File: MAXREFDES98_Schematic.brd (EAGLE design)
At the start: 64.6 x 25.4 mm, 15 parts, among them T1 TG110-S055N2RL

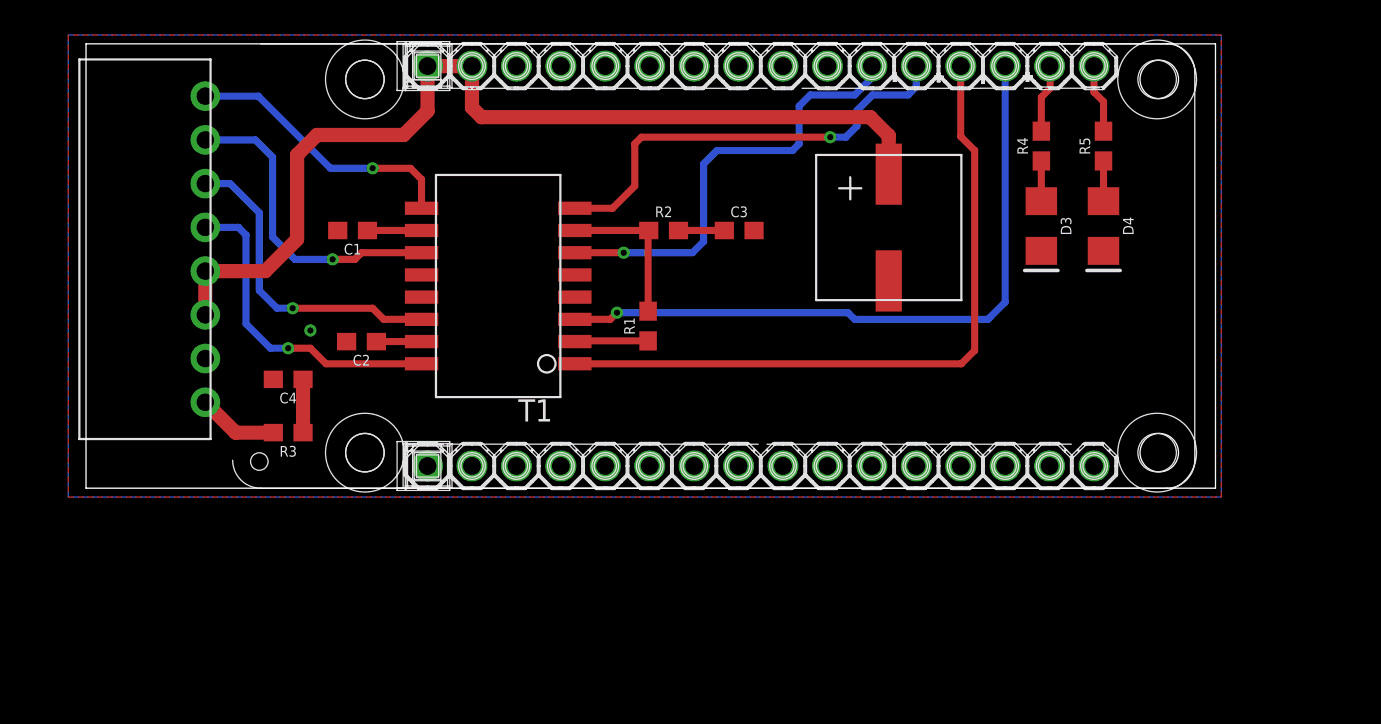
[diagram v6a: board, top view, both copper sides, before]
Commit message: Added schematic labels, 1206 cap, fixed ethernet line width
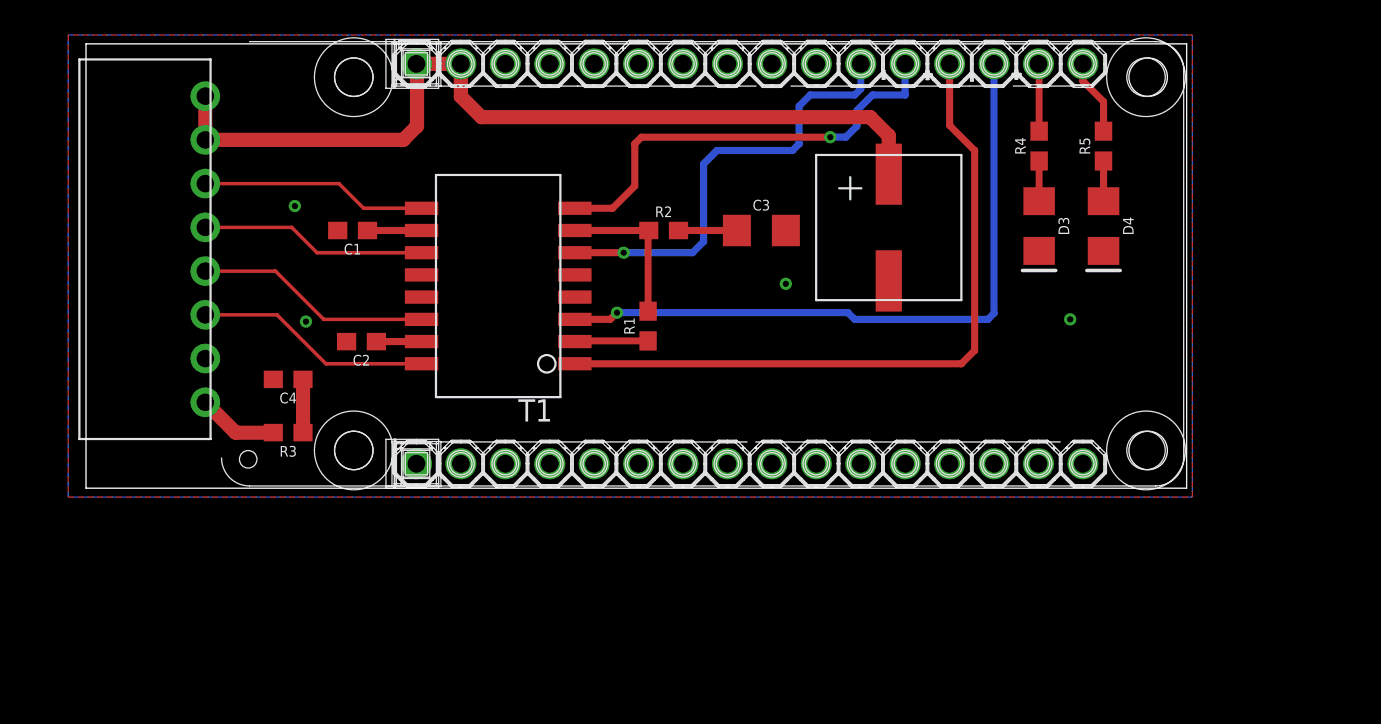
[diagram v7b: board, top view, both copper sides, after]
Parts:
- C3: value 1nF -> 1.0nF; device SparkFun-Capacitors:0603 -> SparkFun-Capacitors:1206
- moved C3 1.27 mm to (40.3, 14.7)
- moved U$2 0.65 mm to (9.40, 25.5)
- moved D3 0.13 mm to (56.1, 15.0)
- moved R4 0.13 mm to (56.1, 19.6)
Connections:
- net 5V_OUT: now also CONN.1, CONN.2; no longer CONN.5, CONN.6
- net RD_N: now also CONN.4; no longer CONN.2
- net RD_P: now also CONN.3; no longer CONN.1
- net TD_N: now also CONN.6; no longer CONN.4
- net TD_P: now also CONN.5; no longer CONN.3
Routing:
- net 5V_OUT: track 56.0 -> 50.5 mm
- net RD_N: track 18.0 -> 13.0 mm, vias 1 -> 0
- net TD_N: track 18.6 -> 13.5 mm, vias 1 -> 0
- net TD_P: track 18.2 -> 13.5 mm, vias 1 -> 0
- net RD_P: track 16.0 -> 12.9 mm, vias 1 -> 0
- net N$3: track 2.62 -> 3.34 mm
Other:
- board size 64.6 x 25.4 mm -> 62.9 x 25.4 mm

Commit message: Added Power Indicator LED, shortened board
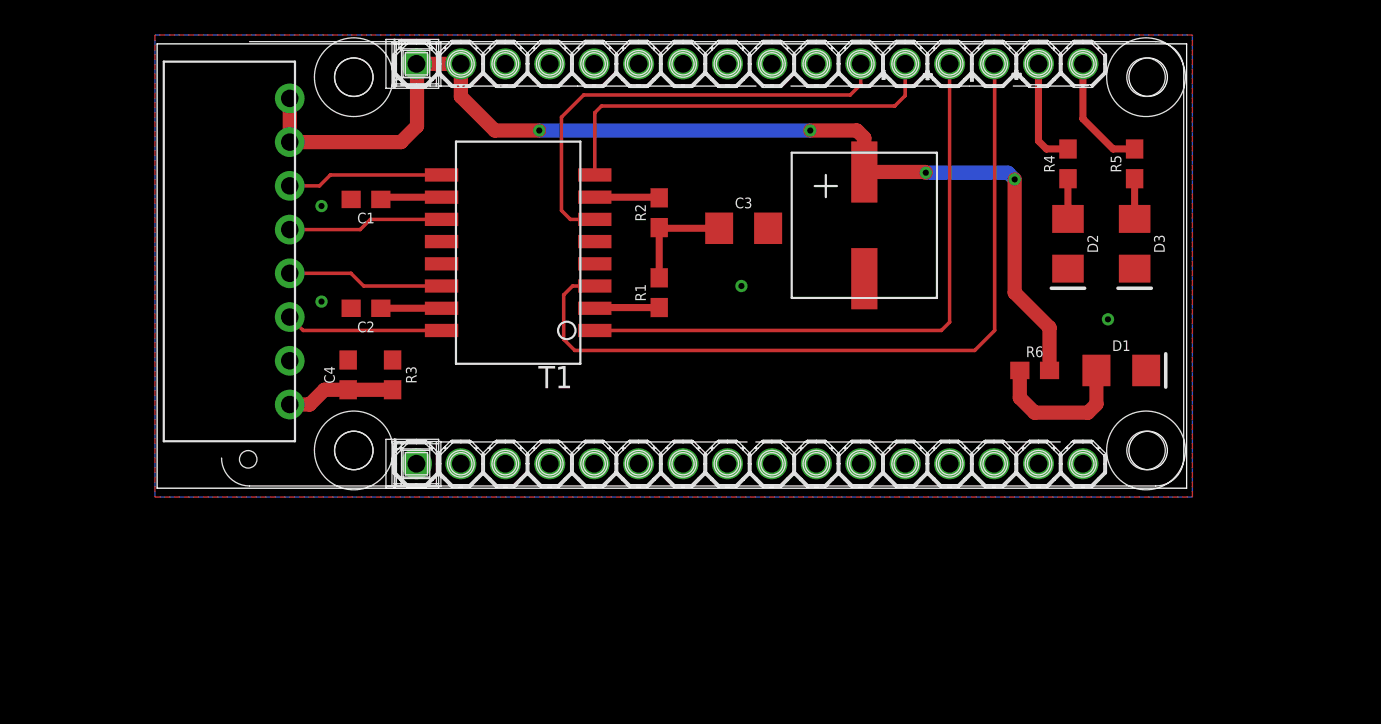
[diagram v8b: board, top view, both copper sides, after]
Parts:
- removed D4: AMBER, SparkFun-LED:FKIT-LED-1206
- added D1: RED, SparkFun-LED:FKIT-LED-1206
- added D2: GREEN, SparkFun-LED:FKIT-LED-1206
- added R6: 470, SparkFun-Resistors:0603
- D3: value GREEN -> AMBER
- moved R3 6.82 mm to (19.2, 6.48), turned to 270 degrees
- moved D3 5.55 mm to (61.6, 14.0)
- moved CONN 4.83 mm to (6.10, 24.4)
- moved C4 3.44 mm to (16.6, 6.48), turned to 90 degrees
- moved T1 2.22 mm to (30.7, 7.11)
- moved R5 2.05 mm to (61.6, 18.5)
- moved R1 2.01 mm to (34.4, 11.2)
- moved R4 1.94 mm to (57.8, 18.5)
- moved C1 1.93 mm to (17.7, 16.5)
- moved C2 1.92 mm to (17.7, 10.3)
- moved C5 1.40 mm to (46.5, 15.4)
- moved R2 1.05 mm to (34.4, 15.7), turned to 90 degrees
- moved C3 1.02 mm to (39.2, 14.9)
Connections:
- removed net N$14: R1.2, R2.1, T1.7
- new net N$5: D1.A, R6.1
- net 5V_OUT: now also R6.2
- net GND: now also D1.C, D2.C, R3.1; no longer D4.C
- net N$1: now also D2.A; no longer D3.A
- net N$2: now also D3.A; no longer D4.A
- net N$3: now also T1.7; no longer C3.1
- net N$4: now also C3.1, R1.2, R2.1; no longer C4.1, R3.1
- net SHIELD: now also C4.1
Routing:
- net 5V_OUT: track 50.5 -> 64.6 mm, vias 0 -> 4
- net N$14: track 8.86 -> 0.00 mm
- net N$5: track 0.00 -> 8.43 mm
- net ETH_TD_P: track 38.7 -> 45.2 mm, vias 1 -> 0
- net ETH_TD_N: track 40.2 -> 35.2 mm
- net TD_P: track 13.5 -> 8.98 mm
- net TD_N: track 13.5 -> 9.00 mm
- net RD_N: track 13.0 -> 8.92 mm
- net RD_P: track 12.9 -> 8.94 mm
- net N$4: track 3.05 -> 6.31 mm
- net SPD: track 4.34 -> 6.81 mm
- net LNK: track 3.86 -> 6.28 mm
- net ETH_RD_P: track 25.3 -> 23.5 mm, vias 1 -> 0
- net SHIELD: track 4.61 -> 6.23 mm
- net ETH_RD_N: track 25.5 -> 26.5 mm, vias 1 -> 0
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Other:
- board size 62.9 x 25.4 mm -> 58.9 x 25.4 mm
